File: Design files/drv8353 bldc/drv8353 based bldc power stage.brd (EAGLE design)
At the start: 85.1 x 131.3 mm, 43 parts

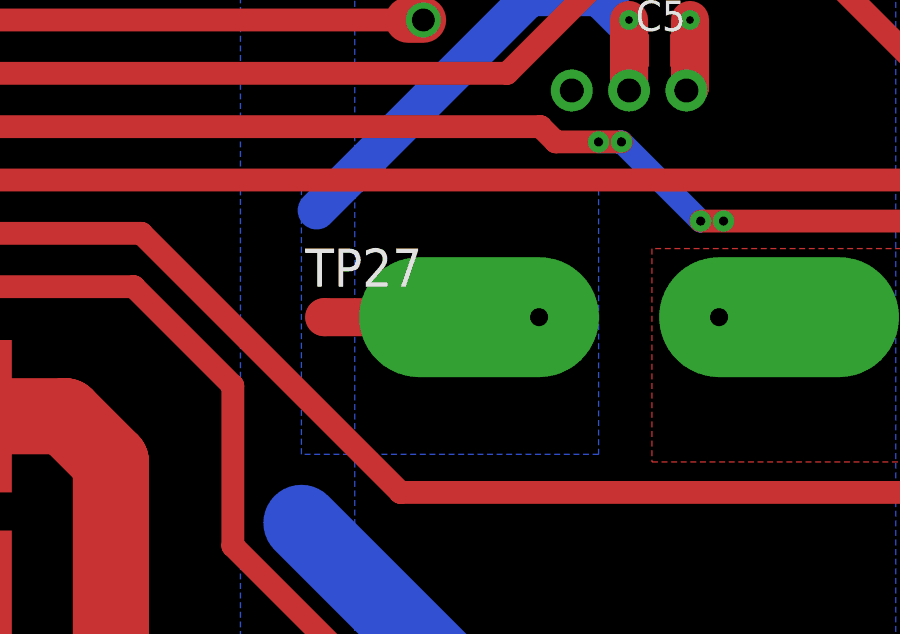
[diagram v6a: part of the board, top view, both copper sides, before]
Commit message: reworked driver stage to work with board interface
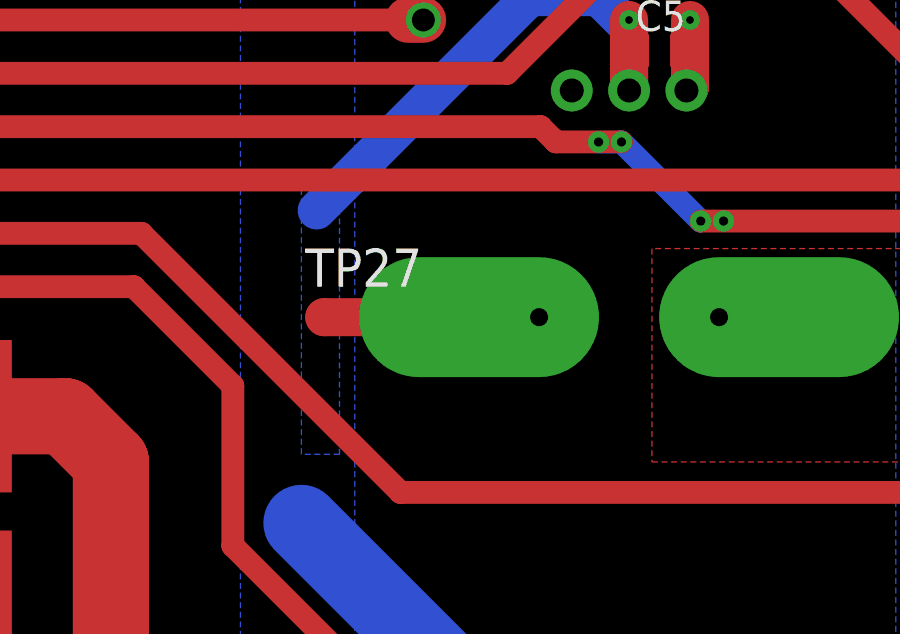
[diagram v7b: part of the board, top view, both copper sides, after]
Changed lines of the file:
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@@
 <polygon width="0" layer="16" thermals="no">
 <vertex x="16.256" y="66.802"/>
-<vertex x="26.162" y="66.802"/>
-<vertex x="26.162" y="57.658"/>
+<vertex x="17.526" y="66.802"/>
+<vertex x="17.526" y="57.658"/>
 <vertex x="16.256" y="57.658"/>
 </polygon>
@@
 <vertex x="6.604" y="50.292"/>
 </polygon>
-<polygon width="0" layer="16">
+<polygon width="0" layer="16" thermals="no">
 <vertex x="14.224" y="130.81"/>
 <vertex x="14.224" y="37.338"/>
@@
 <vertex x="0.254" y="130.81"/>
 </polygon>
-<polygon width="0" layer="2">
+<polygon width="0" layer="2" thermals="no">
 <vertex x="14.224" y="130.81"/>
 <vertex x="14.224" y="37.338"/>
